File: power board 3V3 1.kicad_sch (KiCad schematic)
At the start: 25 parts, among them J1 Conn_02x14_Odd_Even, Q1 NMOS - HL3400A, Q2 PMOS - SI2301, Q3 PMOS - SI2301, U1 TP4056-42-ESOP8, U2 HT7533-1-SOT89, U3 LM358DR

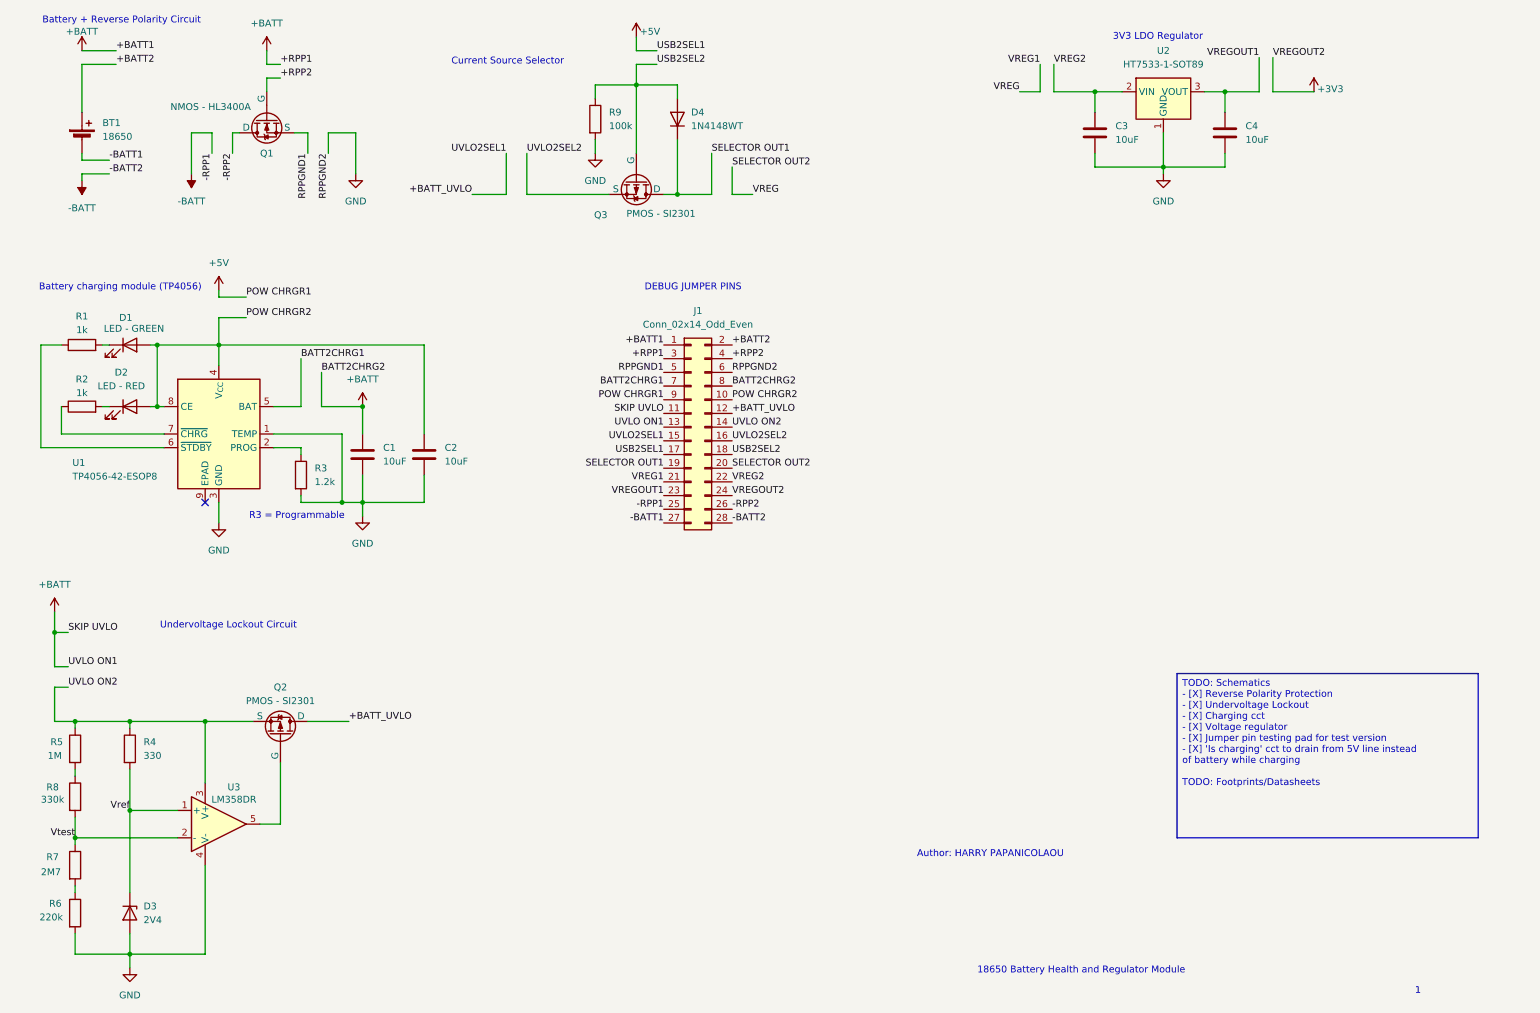
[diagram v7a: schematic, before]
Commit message: Moved test pads
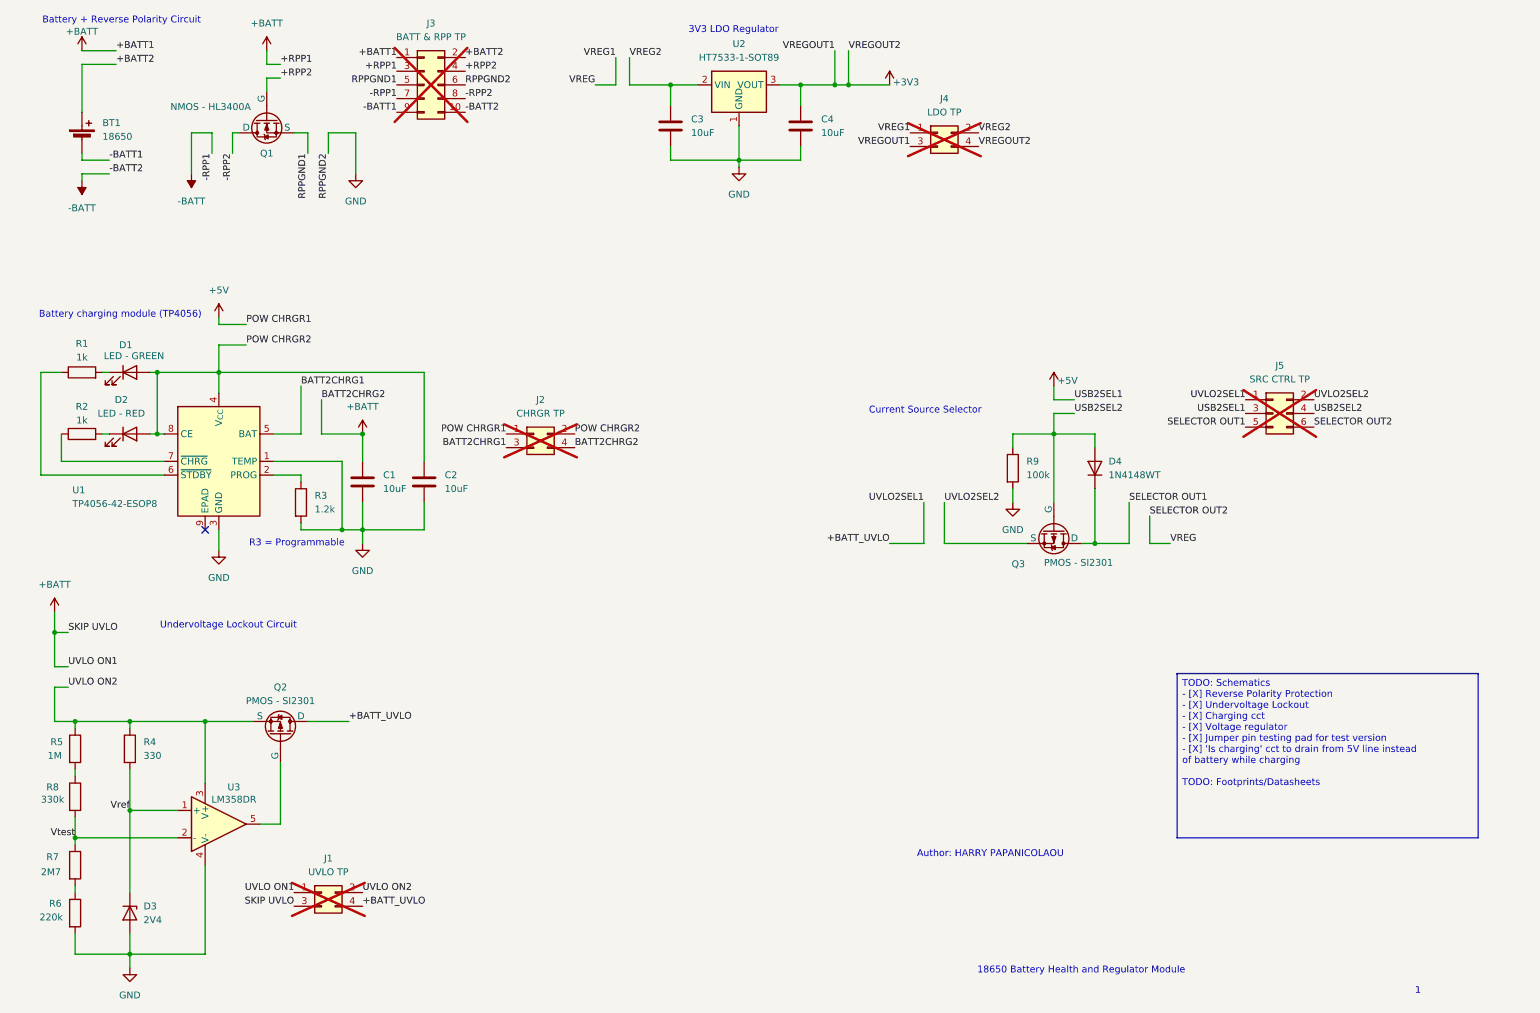
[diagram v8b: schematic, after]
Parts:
- removed J1: Conn_02x14_Odd_Even, Connector_PinHeader_2.54mm:PinHeader_2x14_P2.54mm_Vertical, symbol Connector_Generic:Conn_02x14_Odd_Even
- added J1: UVLO TP, Connector_PinSocket_2.54mm:PinSocket_2x02_P2.54mm_Vertical, symbol Connector_Generic:Conn_02x02_Odd_Even
- added J2: CHRGR TP, Connector_PinSocket_2.54mm:PinSocket_2x02_P2.54mm_Vertical, symbol Connector_Generic:Conn_02x02_Odd_Even
- added J3: BATT & RPP TP, Connector_PinSocket_2.54mm:PinSocket_2x05_P2.54mm_Vertical, symbol Connector_Generic:Conn_02x05_Odd_Even
- added J4: LDO TP, Connector_PinSocket_2.54mm:PinSocket_2x02_P2.54mm_Vertical, symbol Connector_Generic:Conn_02x02_Odd_Even
- added J5: SRC CTRL TP, Connector_PinSocket_2.54mm:PinSocket_2x03_P2.54mm_Vertical, symbol Connector_Generic:Conn_02x03_Odd_Even
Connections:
- net VREGOUT1 is gone; now on net +3V3: C4.1, U2.3 (VOUT)
- net +3V3: now also J4.3 (Pin_3), J4.4 (Pin_4)
- net +5V: now also J2.1 (Pin_1), J5.3 (Pin_3)
- net +BATT: now also J1.1 (Pin_1), J1.3 (Pin_3), J2.4 (Pin_4), J3.1 (Pin_1), J3.3 (Pin_3)
- net +BATT2: now also J3.2 (Pin_2)
- net +BATT_UVLO: now also J1.4 (Pin_4), J5.1 (Pin_1)
- net +RPP2: now also J3.4 (Pin_4)
- net -BATT: now also J3.10 (Pin_10), J3.7 (Pin_7)
- net -BATT1: now also J3.9 (Pin_9)
- net -RPP2: now also J3.8 (Pin_8)
- net BATT2CHRG1: now also J2.3 (Pin_3)
- net GND: now also J3.6 (Pin_6)
- net POW CHRGR2: now also J2.2 (Pin_2)
- net RPPGND1: now also J3.5 (Pin_5)
- net SELECTOR OUT1: now also J5.5 (Pin_5)
- net SELECTOR OUT2: now also J4.1 (Pin_1), J5.6 (Pin_6)
- net USB2SEL2: now also J5.4 (Pin_4)
- net UVLO ON2: now also J1.2 (Pin_2)
- net UVLO2SEL2: now also J5.2 (Pin_2)
- net VREG2: now also J4.2 (Pin_2)
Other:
- note removed: "DEBUG JUMPER PINS"
- moved on the sheet: C1, C2, C3, C4, D1, D2, D4, Q3, R1, R2, R3, R9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
